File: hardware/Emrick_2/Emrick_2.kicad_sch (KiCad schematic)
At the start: 11 parts, among them J1 BATT_CONN, J2 LED_CONN, SW1 SW_SPST, SW2 SW_Push_LED

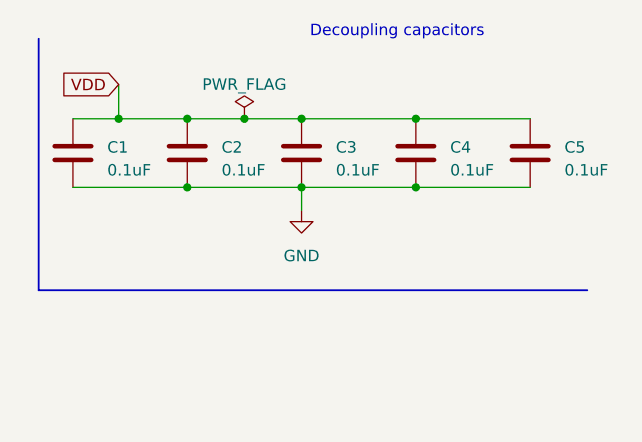
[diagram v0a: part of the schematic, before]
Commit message: Updated power flags and decoupling capacitors for 5V and gnd
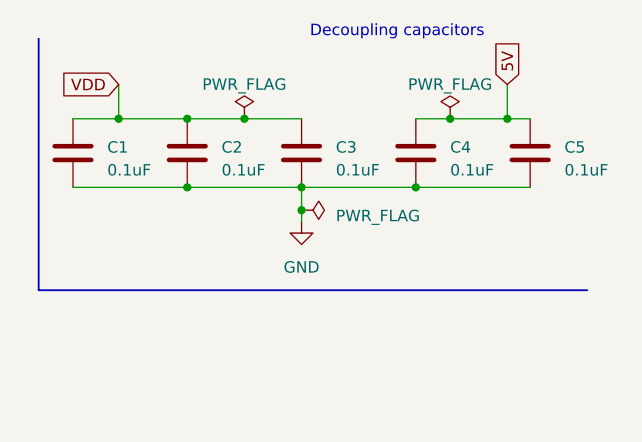
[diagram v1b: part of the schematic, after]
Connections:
- net 5V: now also C4.2, C5.2
- net VDD: no longer C4.2, C5.2
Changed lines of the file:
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@@
   (junction (at 106.68 34.29) (diameter 0) (color 0 0 0 0)
   )
-  (junction (at 262.89 24.13) (diameter 0) (color 0 0 0 0)
-  )
   (junction (at 262.89 31.75) (diameter 0) (color 0 0 0 0)
   )
   (junction (at 38.1 57.15) (diameter 0) (color 0 0 0 0)
   )
+  (junction (at 273.05 24.13) (diameter 0) (color 0 0 0 0)
+  )
   (junction (at 237.49 31.75) (diameter 0) (color 0 0 0 0)
   )
   (junction (at 237.49 24.13) (diameter 0) (color 0 0 0 0)
   )
+  (junction (at 266.7 24.13) (diameter 0) (color 0 0 0 0)
+  )
   (junction (at 80.01 31.75) (diameter 0) (color 0 0 0 0)
   )
   (junction (at 250.19 31.75) (diameter 0) (color 0 0 0 0)
   )
-  (junction (at 250.19 24.13) (diameter 0) (color 0 0 0 0)
+  (junction (at 250.19 34.29) (diameter 0) (color 0 0 0 0)
   )
   (junction (at 243.84 24.13) (diameter 0) (color 0 0 0 0)
@@
     (stroke (width 0) (type default))
   )
-  (wire (pts (xy 262.89 24.13) (xy 275.59 24.13))
+  (wire (pts (xy 262.89 24.13) (xy 266.7 24.13))
     (stroke (width 0) (type default))
   )
@@
     (stroke (width 0) (type default))
   )
-  (wire (pts (xy 250.19 24.13) (xy 262.89 24.13))
-    (stroke (width 0) (type default))
-  )
   (wire (pts (xy 38.1 57.15) (xy 39.37 57.15))
     (stroke (width 0) (type default))
@@
     (stroke (width 0) (type default))
   )
+  (wire (pts (xy 250.19 35.56) (xy 250.19 34.29))
+    (stroke (width 0) (type default))
+  )
+  (wire (pts (xy 273.05 24.13) (xy 275.59 24.13))
+    (stroke (width 0) (type default))
+  )
   (wire (pts (xy 39.37 49.53) (xy 38.1 49.53))
     (stroke (width 0) (type default))
@@
     (stroke (width 0) (type default))
   )
+  (wire (pts (xy 266.7 24.13) (xy 273.05 24.13))
+    (stroke (width 0) (type default))
+  )
   (polyline (pts (xy 220.98 15.24) (xy 220.98 43.18))
     (stroke (width 0.2) (type default))
@@
   )
   (wire (pts (xy 106.68 34.29) (xy 106.68 36.83))
+    (stroke (width 0) (type default))
+  )
+  (wire (pts (xy 273.05 20.32) (xy 273.05 24.13))
     (stroke (width 0) (type default))
   )
@@
     )
   )
+  (global_label "5V" (shape input) (at 273.05 20.32 90) (fields_autoplaced)
+    (effects (font (size 1.27 1.27)) (justify left))
+    (property "Intersheetrefs" "${INTERSHEET_REFS}" (at 273.05 15.1161 90)
+      (effects (font (size 1.27 1.27)) (justify left) hide)
+    )
+  )
   (global_label "BTN_INPUT" (shape input) (at 80.01 30.48 90) (fields_autoplaced)
     (effects (font (size 1.27 1.27)) (justify left))
@@
     )
   )
+  (symbol (lib_id "power:PWR_FLAG") (at 266.7 24.13 0) (unit 1)
+    (in_bom yes) (on_board yes) (dnp no) (fields_autoplaced)
+    (property "Reference" "#FLG03" (at 266.7 22.225 0)
+      (effects (font (size 1.27 1.27)) hide)
+    )
+    (property "Value" "PWR_FLAG" (at 266.7 20.32 0)
+      (effects (font (size 1.27 1.27)))
+    )
+    (property "Footprint" "" (at 266.7 24.13 0)
+      (effects (font (size 1.27 1.27)) hide)
+    )
+    (property "Datasheet" "~" (at 266.7 24.13 0)
+      (effects (font (size 1.27 1.27)) hide)
+    )
+    (pin "1")
+    (instances
+      (project "Emrick_2"
+        (path "/92ce4ab8-4759-4464-a4e8-9ba226cea402"
+          (reference "#FLG03") (unit 1)
+        )
+      )
+    )
+  )
+  (symbol (lib_id "power:PWR_FLAG") (at 250.19 34.29 270) (unit 1)
+    (in_bom yes) (on_board yes) (dnp no) (fields_autoplaced)
+    (property "Reference" "#FLG02" (at 252.095 34.29 0)
+      (effects (font (size 1.27 1.27)) hide)
+    )
+    (property "Value" "PWR_FLAG" (at 254 34.925 90)
+      (effects (font (size 1.27 1.27)) (justify left))
+    )
+    (property "Footprint" "" (at 250.19 34.29 0)
+      (effects (font (size 1.27 1.27)) hide)
+    )
+    (property "Datasheet" "~" (at 250.19 34.29 0)
+      (effects (font (size 1.27 1.27)) hide)
+    )
+    (pin "1")
+    (instances
+      (project "Emrick_2"
+        (path "/92ce4ab8-4759-4464-a4e8-9ba226cea402"
+          (reference "#FLG02") (unit 1)
+        )
+      )
+    )
+  )
   (symbol (lib_id "power:GND") (at 35.56 31.75 270) (unit 1)
     (in_bom yes) (on_board yes) (dnp no) (fields_autoplaced)
@@
     )
   )
-  (symbol (lib_id "power:GND") (at 250.19 34.29 0) (unit 1)
-    (in_bom yes) (on_board yes) (dnp no) (fields_autoplaced)
-    (property "Reference" "#PWR01" (at 250.19 40.64 0)
-      (effects (font (size 1.27 1.27)) hide)
-    )
-    (property "Value" "GND" (at 250.19 39.37 0)
+  (symbol (lib_id "power:GND") (at 250.19 35.56 0) (unit 1)
+    (in_bom yes) (on_board yes) (dnp no) (fields_autoplaced)
+    (property "Reference" "#PWR01" (at 250.19 41.91 0)
+      (effects (font (size 1.27 1.27)) hide)
+    )
+    (property "Value" "GND" (at 250.19 40.64 0)
       (effects (font (size 1.27 1.27)))
     )
-    (property "Footprint" "" (at 250.19 34.29 0)
-      (effects (font (size 1.27 1.27)) hide)
-    )
-    (property "Datasheet" "" (at 250.19 34.29 0)
-      (effects (font (size 1.27 1.27)) hide)
-    )
+    (property "Footprint" "" (at 250.19 35.56 0)
+      (effects (font (size 1.27 1.27)) hide)
+    )
+    (property "Datasheet" "" (at 250.19 35.56 0)
+      (effects (font (size 1.27 1.27)) hide)
+    )
